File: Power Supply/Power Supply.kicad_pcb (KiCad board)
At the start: 2 copper layers, 84 x 96 mm, 37 parts, among them U1 LT3086ET7, U2 LT3091ET7

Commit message: Finish up power supply
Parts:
- moved D3 3.09 mm to (144.8, 102.2)
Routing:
- net -12V: track 23.2 -> 19.9 mm
- net +12V: track 40.6 -> 43.8 mm
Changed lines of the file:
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@@
   )
   (footprint "Diode_THT:D_DO-41_SOD81_P10.16mm_Horizontal" (layer "F.Cu")
-    (at 142.22 100.55 180)
+    (at 144.8 102.25 180)
     (descr "Diode, DO-41_SOD81 series, Axial, Horizontal, pin pitch=10.16mm, , length*diameter=5.2*2.7mm^2, , http://www.diodes.com/_files/packages/DO-41%20(Plastic).pdf")
     (tags "Diode DO-41_SOD81 series Axial Horizontal pin pitch 10.16mm  length 5.2mm diameter 2.7mm")
@@
   (segment (start 159.226953 66.25) (end 159.738477 65.738476) (width 2.25) (layer "F.Cu") (net 5))
   (segment (start 163.025 72.48) (end 160.1 72.48) (width 2.25) (layer "F.Cu") (net 5))
+  (segment (start 150.13 93.85) (end 151.6 93.85) (width 2.25) (layer "F.Cu") (net 5))
   (segment (start 157.652602 67.824351) (end 158.488477 66.988476) (width 2.25) (layer "F.Cu") (net 5))
   (segment (start 159.185204 72.48) (end 157.652602 70.947398) (width 2.25) (layer "F.Cu") (net 5))
@@
   (segment (start 153.855 71.255) (end 152.3 72.81) (width 2.25) (layer "F.Cu") (net 5))
   (segment (start 153.855 71.255) (end 154.735 70.375) (width 2.25) (layer "F.Cu") (net 5))
-  (segment (start 150.13 93.85) (end 156.75 93.85) (width 2.25) (layer "F.Cu") (net 5))
   (segment (start 156.2 70) (end 156.2 66.3) (width 2.25) (layer "F.Cu") (net 5))
+  (segment (start 150.13 96.41) (end 150.13 95.32) (width 2.25) (layer "F.Cu") (net 5))
+  (segment (start 150.13 95.32) (end 151.6 93.85) (width 2.25) (layer "F.Cu") (net 5))
   (segment (start 156.2 70) (end 155.11 70) (width 2.25) (layer "F.Cu") (net 5))
   (segment (start 157.080204 70.375) (end 157.652602 70.947398) (width 2.25) (layer "F.Cu") (net 5))
@@
   (segment (start 159.136953 66.34) (end 159.226953 66.25) (width 2.25) (layer "F.Cu") (net 5))
   (segment (start 154.735 70.375) (end 157.080204 70.375) (width 2.25) (layer "F.Cu") (net 5))
+  (segment (start 151.6 93.85) (end 156.75 93.85) (width 2.25) (layer "F.Cu") (net 5))
   (segment (start 161.735 132.35) (end 163.025 131.06) (width 2.25) (layer "F.Cu") (net 6))
   (segment (start 159.89 132.35) (end 161.735 132.35) (width 2.25) (layer "F.Cu") (net 6))
   (segment (start 150.14 107.35) (end 157.4 107.35) (width 2.25) (layer "F.Cu") (net 6))
-  (segment (start 142.22 100.55) (end 143.92 102.25) (width 2.25) (layer "F.Cu") (net 6))
   (segment (start 147.59 102.25) (end 150.14 104.8) (width 2.25) (layer "F.Cu") (net 6))
   (segment (start 150.14 104.8) (end 150.14 107.35) (width 2.25) (layer "F.Cu") (net 6))
-  (segment (start 143.92 102.25) (end 147.59 102.25) (width 2.25) (layer "F.Cu") (net 6))
+  (segment (start 147.59 102.25) (end 144.8 102.25) (width 2.25) (layer "F.Cu") (net 6))
   (segment (start 166.45 80.05) (end 169.175 77.325) (width 2.25) (layer "F.Cu") (net 7))
   (segment (start 152.34 77.9) (end 154.49 80.05) (width 2.25) (layer "F.Cu") (net 7))
@@
     (polygon
       (pts
-        (xy 114.9 98.5)
-        (xy 114.9 135)
-        (xy 142 135)
-        (xy 142 98.5)
+        (xy 114.9 99.9)
+        (xy 114.9 133.9)
+        (xy 142 133.9)
+        (xy 142 99.9)
       )
     )
@@
         (xy 102 149.05)
         (xy 102 91)
-        (xy 102 58.5)
-        (xy 142.25 58.5)
+        (xy 102 51.75)
+        (xy 142.25 51.75)
         (xy 142.25 98)
-        (xy 114.4 98)
-        (xy 114.4 135.7)
-        (xy 121.6 135.7)
-        (xy 121.6 149.05)
+        (xy 113.1 98)
+        (xy 113.1 135.7)
+        (xy 120.8 135.7)
+        (xy 120.8 149.05)
       )
     )
@@
         (xy 154.75 52)
         (xy 154.75 62.5)
-        (xy 154.75 62.5)
         (xy 154.75 69)

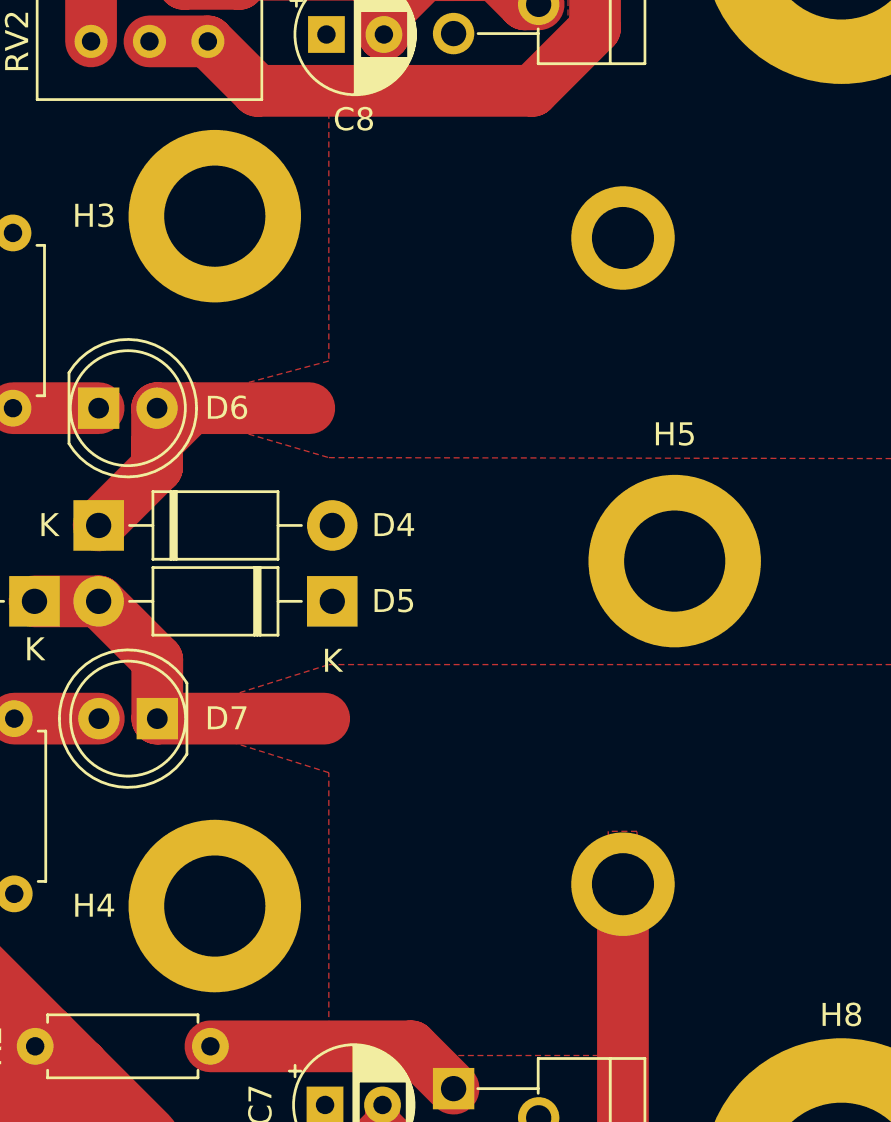
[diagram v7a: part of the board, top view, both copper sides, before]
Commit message: Add vias to PSU screw holes
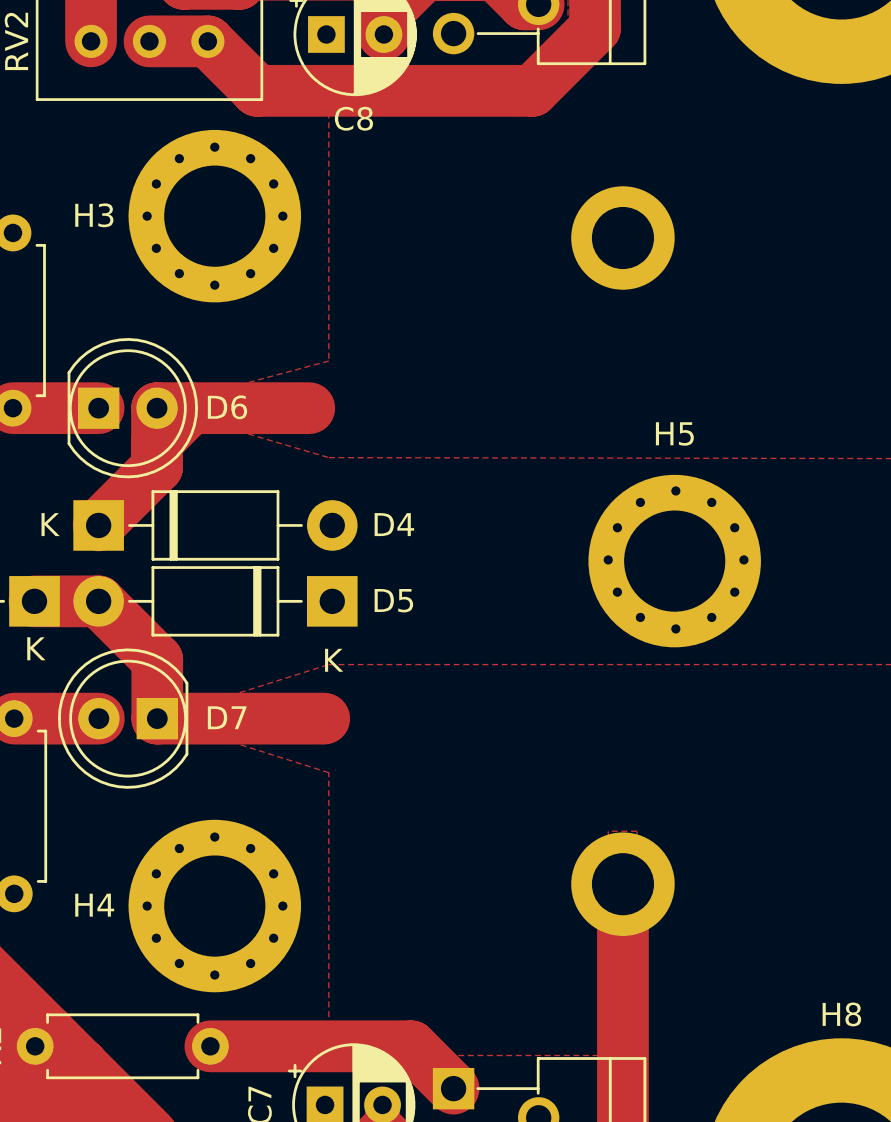
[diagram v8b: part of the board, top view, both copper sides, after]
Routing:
- net GND: track 0.00 -> 58.0 mm, vias 0 -> 36
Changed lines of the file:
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@@
   (segment (start 149.8 71.875177) (end 147.324823 69.4) (width 2.25) (layer "F.Cu") (net 1))
   (segment (start 149.8 73.9) (end 149.8 72.3) (width 2.25) (layer "F.Cu") (net 1))
+  (via (at 154.2 83) (size 0.8) (drill 0.4) (layers "F.Cu" "B.Cu") (free) (net 2))
+  (via (at 174.25 97.95) (size 0.8) (drill 0.4) (layers "F.Cu" "B.Cu") (free) (net 2))
+  (via (at 155.6 115.5) (size 0.8) (drill 0.4) (layers "F.Cu" "B.Cu") (free) (net 2))
+  (via (at 175.25 101.85) (size 0.8) (drill 0.4) (layers "F.Cu" "B.Cu") (free) (net 2))
+  (via (at 155.2 116.9) (size 0.8) (drill 0.4) (layers "F.Cu" "B.Cu") (free) (net 2))
+  (via (at 154.2 118) (size 0.8) (drill 0.4) (layers "F.Cu" "B.Cu") (free) (net 2))
+  (via (at 151.1 118) (size 0.8) (drill 0.4) (layers "F.Cu" "B.Cu") (free) (net 2))
+  (via (at 155.2 86.9) (size 0.8) (drill 0.4) (layers "F.Cu" "B.Cu") (free) (net 2))
+  (via (at 172.69 103.45) (size 0.8) (drill 0.4) (layers "F.Cu" "B.Cu") (free) (net 2))
+  (via (at 155.2 84.1) (size 0.8) (drill 0.4) (layers "F.Cu" "B.Cu") (free) (net 2))
+  (via (at 150.1 114.1) (size 0.8) (drill 0.4) (layers "F.Cu" "B.Cu") (free) (net 2))
+  (via (at 152.64 88.5) (size 0.8) (drill 0.4) (layers "F.Cu" "B.Cu") (free) (net 2))
+  (via (at 155.6 85.5) (size 0.8) (drill 0.4) (layers "F.Cu" "B.Cu") (free) (net 2))
+  (via (at 149.7 115.5) (size 0.8) (drill 0.4) (layers "F.Cu" "B.Cu") (free) (net 2))
+  (via (at 172.69 97.45) (size 0.8) (drill 0.4) (layers "F.Cu" "B.Cu") (free) (net 2))
+  (via (at 152.64 118.5) (size 0.8) (drill 0.4) (layers "F.Cu" "B.Cu") (free) (net 2))
+  (via (at 171.15 102.95) (size 0.8) (drill 0.4) (layers "F.Cu" "B.Cu") (free) (net 2))
+  (via (at 169.75 100.45) (size 0.8) (drill 0.4) (layers "F.Cu" "B.Cu") (free) (net 2))
+  (via (at 155.2 114.1) (size 0.8) (drill 0.4) (layers "F.Cu" "B.Cu") (free) (net 2))
+  (via (at 154.2 113) (size 0.8) (drill 0.4) (layers "F.Cu" "B.Cu") (free) (net 2))
+  (via (at 150.1 86.9) (size 0.8) (drill 0.4) (layers "F.Cu" "B.Cu") (free) (net 2))
+  (via (at 174.25 102.95) (size 0.8) (drill 0.4) (layers "F.Cu" "B.Cu") (free) (net 2))
+  (via (at 149.7 85.5) (size 0.8) (drill 0.4) (layers "F.Cu" "B.Cu") (free) (net 2))
+  (via (at 150.1 84.1) (size 0.8) (drill 0.4) (layers "F.Cu" "B.Cu") (free) (net 2))
+  (via (at 152.64 112.5) (size 0.8) (drill 0.4) (layers "F.Cu" "B.Cu") (free) (net 2))
+  (via (at 171.15 97.95) (size 0.8) (drill 0.4) (layers "F.Cu" "B.Cu") (free) (net 2))
+  (via (at 175.25 99.05) (size 0.8) (drill 0.4) (layers "F.Cu" "B.Cu") (free) (net 2))
+  (via (at 151.1 88) (size 0.8) (drill 0.4) (layers "F.Cu" "B.Cu") (free) (net 2))
+  (via (at 151.1 83) (size 0.8) (drill 0.4) (layers "F.Cu" "B.Cu") (free) (net 2))
+  (via (at 154.2 88) (size 0.8) (drill 0.4) (layers "F.Cu" "B.Cu") (free) (net 2))
+  (via (at 152.64 82.5) (size 0.8) (drill 0.4) (layers "F.Cu" "B.Cu") (free) (net 2))
+  (via (at 175.65 100.45) (size 0.8) (drill 0.4) (layers "F.Cu" "B.Cu") (free) (net 2))
+  (via (at 150.1 116.9) (size 0.8) (drill 0.4) (layers "F.Cu" "B.Cu") (free) (net 2))
+  (via (at 170.15 99.05) (size 0.8) (drill 0.4) (layers "F.Cu" "B.Cu") (free) (net 2))
+  (via (at 151.1 113) (size 0.8) (drill 0.4) (layers "F.Cu" "B.Cu") (free) (net 2))
+  (via (at 170.15 101.85) (size 0.8) (drill 0.4) (layers "F.Cu" "B.Cu") (free) (net 2))
+  (segment (start 155.2 84.1) (end 155.2 84) (width 0.3) (layer "B.Cu") (net 2))
+  (segment (start 155.6 116.5) (end 155.2 116.9) (width 0.3) (layer "B.Cu") (net 2))
+  (segment (start 155.6 115.5) (end 155.6 114.5) (width 0.3) (layer "B.Cu") (net 2))
+  (segment (start 149.7 84.5) (end 150.1 84.1) (width 0.3) (layer "B.Cu") (net 2))
+  (segment (start 155.2 116.9) (end 155.2 117) (width 0.3) (layer "B.Cu") (net 2))
+  (segment (start 169.75 100.45) (end 169.75 99.45) (width 0.3) (layer "B.Cu") (net 2))
+  (segment (start 150.1 116.9) (end 150.1 117) (width 0.3) (layer "B.Cu") (net 2))
+  (segment (start 150.1 84.1) (end 150.1 84) (width 0.3) (layer "B.Cu") (net 2))
+  (segment (start 169.75 99.45) (end 170.15 99.05) (width 0.3) (layer "B.Cu") (net 2))
+  (segment (start 175.65 99.45) (end 175.25 99.05) (width 0.3) (layer "B.Cu") (net 2))
+  (segment (start 171.65 103.45) (end 171.15 102.95) (width 0.3) (layer "B.Cu") (net 2))
+  (segment (start 152.64 118.5) (end 151.6 118.5) (width 0.3) (layer "B.Cu") (net 2))
+  (segment (start 175.25 101.85) (end 175.25 101.95) (width 0.3) (layer "B.Cu") (net 2))
+  (segment (start 173.75 103.45) (end 174.25 102.95) (width 0.3) (layer "B.Cu") (net 2))
+  (segment (start 155.6 85.5) (end 155.6 84.5) (width 0.3) (layer "B.Cu") (net 2))
+  (segment (start 155.6 114.5) (end 155.2 114.1) (width 0.3) (layer "B.Cu") (net 2))
+  (segment (start 150.1 86.9) (end 150.1 87) (width 0.3) (layer "B.Cu") (net 2))
+  (segment (start 155.6 84.5) (end 155.2 84.1) (width 0.3) (layer "B.Cu") (net 2))
+  (segment (start 151.6 112.5) (end 151.1 113) (width 0.3) (layer "B.Cu") (net 2))
+  (segment (start 149.7 86.5) (end 150.1 86.9) (width 0.3) (layer "B.Cu") (net 2))
+  (segment (start 155.2 84) (end 154.2 83) (width 0.3) (layer "B.Cu") (net 2))
+  (segment (start 149.7 115.5) (end 149.7 114.5) (width 0.3) (layer "B.Cu") (net 2))
+  (segment (start 175.65 101.45) (end 175.25 101.85) (width 0.3) (layer "B.Cu") (net 2))
+  (segment (start 155.2 117) (end 154.2 118) (width 0.3) (layer "B.Cu") (net 2))
+  (segment (start 151.6 88.5) (end 151.1 88) (width 0.3) (layer "B.Cu") (net 2))
+  (segment (start 175.65 100.45) (end 175.65 101.45) (width 0.3) (layer "B.Cu") (net 2))
+  (segment (start 149.7 115.5) (end 149.7 116.5) (width 0.3) (layer "B.Cu") (net 2))
+  (segment (start 150.1 84) (end 151.1 83) (width 0.3) (layer "B.Cu") (net 2))
+  (segment (start 152.64 82.5) (end 153.7 82.5) (width 0.3) (layer "B.Cu") (net 2))
+  (segment (start 169.75 100.45) (end 169.75 101.45) (width 0.3) (layer "B.Cu") (net 2))
+  (segment (start 155.6 115.5) (end 155.6 116.5) (width 0.3) (layer "B.Cu") (net 2))
+  (segment (start 155.6 85.5) (end 155.6 86.5) (width 0.3) (layer "B.Cu") (net 2))
+  (segment (start 171.65 97.45) (end 171.15 97.95) (width 0.3) (layer "B.Cu") (net 2))
+  (segment (start 151.6 82.5) (end 151.1 83) (width 0.3) (layer "B.Cu") (net 2))
+  (segment (start 150.1 114.1) (end 150.1 114) (width 0.3) (layer "B.Cu") (net 2))
+  (segment (start 152.64 88.5) (end 151.6 88.5) (width 0.3) (layer "B.Cu") (net 2))
+  (segment (start 150.1 117) (end 151.1 118) (width 0.3) (layer "B.Cu") (net 2))
+  (segment (start 172.69 97.45) (end 173.75 97.45) (width 0.3) (layer "B.Cu") (net 2))
+  (segment (start 155.2 114) (end 154.2 113) (width 0.3) (layer "B.Cu") (net 2))
+  (segment (start 151.6 118.5) (end 151.1 118) (width 0.3) (layer "B.Cu") (net 2))
+  (segment (start 170.15 101.95) (end 171.15 102.95) (width 0.3) (layer "B.Cu") (net 2))
+  (segment (start 152.64 118.5) (end 153.7 118.5) (width 0.3) (layer "B.Cu") (net 2))
+  (segment (start 172.69 103.45) (end 173.75 103.45) (width 0.3) (layer "B.Cu") (net 2))
+  (segment (start 153.7 118.5) (end 154.2 118) (width 0.3) (layer "B.Cu") (net 2))
+  (segment (start 170.15 101.85) (end 170.15 101.95) (width 0.3) (layer "B.Cu") (net 2))
+  (segment (start 149.7 116.5) (end 150.1 116.9) (width 0.3) (layer "B.Cu") (net 2))
+  (segment (start 152.64 88.5) (end 153.7 88.5) (width 0.3) (layer "B.Cu") (net 2))
+  (segment (start 170.15 98.95) (end 171.15 97.95) (width 0.3) (layer "B.Cu") (net 2))
+  (segment (start 173.75 97.45) (end 174.25 97.95) (width 0.3) (layer "B.Cu") (net 2))
+  (segment (start 149.7 85.5) (end 149.7 84.5) (width 0.3) (layer "B.Cu") (net 2))
+  (segment (start 172.69 103.45) (end 171.65 103.45) (width 0.3) (layer "B.Cu") (net 2))
+  (segment (start 152.64 112.5) (end 153.7 112.5) (width 0.3) (layer "B.Cu") (net 2))
+  (segment (start 169.75 101.45) (end 170.15 101.85) (width 0.3) (layer "B.Cu") (net 2))
+  (segment (start 155.2 86.9) (end 155.2 87) (width 0.3) (layer "B.Cu") (net 2))
+  (segment (start 175.65 100.45) (end 175.65 99.45) (width 0.3) (layer "B.Cu") (net 2))
+  (segment (start 153.7 112.5) (end 154.2 113) (width 0.3) (layer "B.Cu") (net 2))
+  (segment (start 155.2 87) (end 154.2 88) (width 0.3) (layer "B.Cu") (net 2))
+  (segment (start 152.64 112.5) (end 151.6 112.5) (width 0.3) (layer "B.Cu") (net 2))
+  (segment (start 175.25 101.95) (end 174.25 102.95) (width 0.3) (layer "B.Cu") (net 2))
+  (segment (start 150.1 87) (end 151.1 88) (width 0.3) (layer "B.Cu") (net 2))
+  (segment (start 155.2 114.1) (end 155.2 114) (width 0.3) (layer "B.Cu") (net 2))
+  (segment (start 175.25 98.95) (end 174.25 97.95) (width 0.3) (layer "B.Cu") (net 2))
+  (segment (start 152.64 82.5) (end 151.6 82.5) (width 0.3) (layer "B.Cu") (net 2))
+  (segment (start 175.25 99.05) (end 175.25 98.95) (width 0.3) (layer "B.Cu") (net 2))
+  (segment (start 170.15 99.05) (end 170.15 98.95) (width 0.3) (layer "B.Cu") (net 2))
+  (segment (start 155.6 86.5) (end 155.2 86.9) (width 0.3) (layer "B.Cu") (net 2))
+  (segment (start 149.7 85.5) (end 149.7 86.5) (width 0.3) (layer "B.Cu") (net 2))
+  (segment (start 150.1 114) (end 151.1 113) (width 0.3) (layer "B.Cu") (net 2))
+  (segment (start 153.7 88.5) (end 154.2 88) (width 0.3) (layer "B.Cu") (net 2))
+  (segment (start 153.7 82.5) (end 154.2 83) (width 0.3) (layer "B.Cu") (net 2))
+  (segment (start 172.69 97.45) (end 171.65 97.45) (width 0.3) (layer "B.Cu") (net 2))
+  (segment (start 149.7 114.5) (end 150.1 114.1) (width 0.3) (layer "B.Cu") (net 2))
   (segment (start 141.75 123.5) (end 139.75 125.5) (width 4) (layer "F.Cu") (net 3))
   (segment (start 140.73 117.5) (end 144.83 121.6) (width 4) (layer "F.Cu") (net 3))
